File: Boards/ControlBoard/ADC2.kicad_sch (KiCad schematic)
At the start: 34 parts, among them IC3 MAX22530AWE+, IC4 MAX22530AWE+

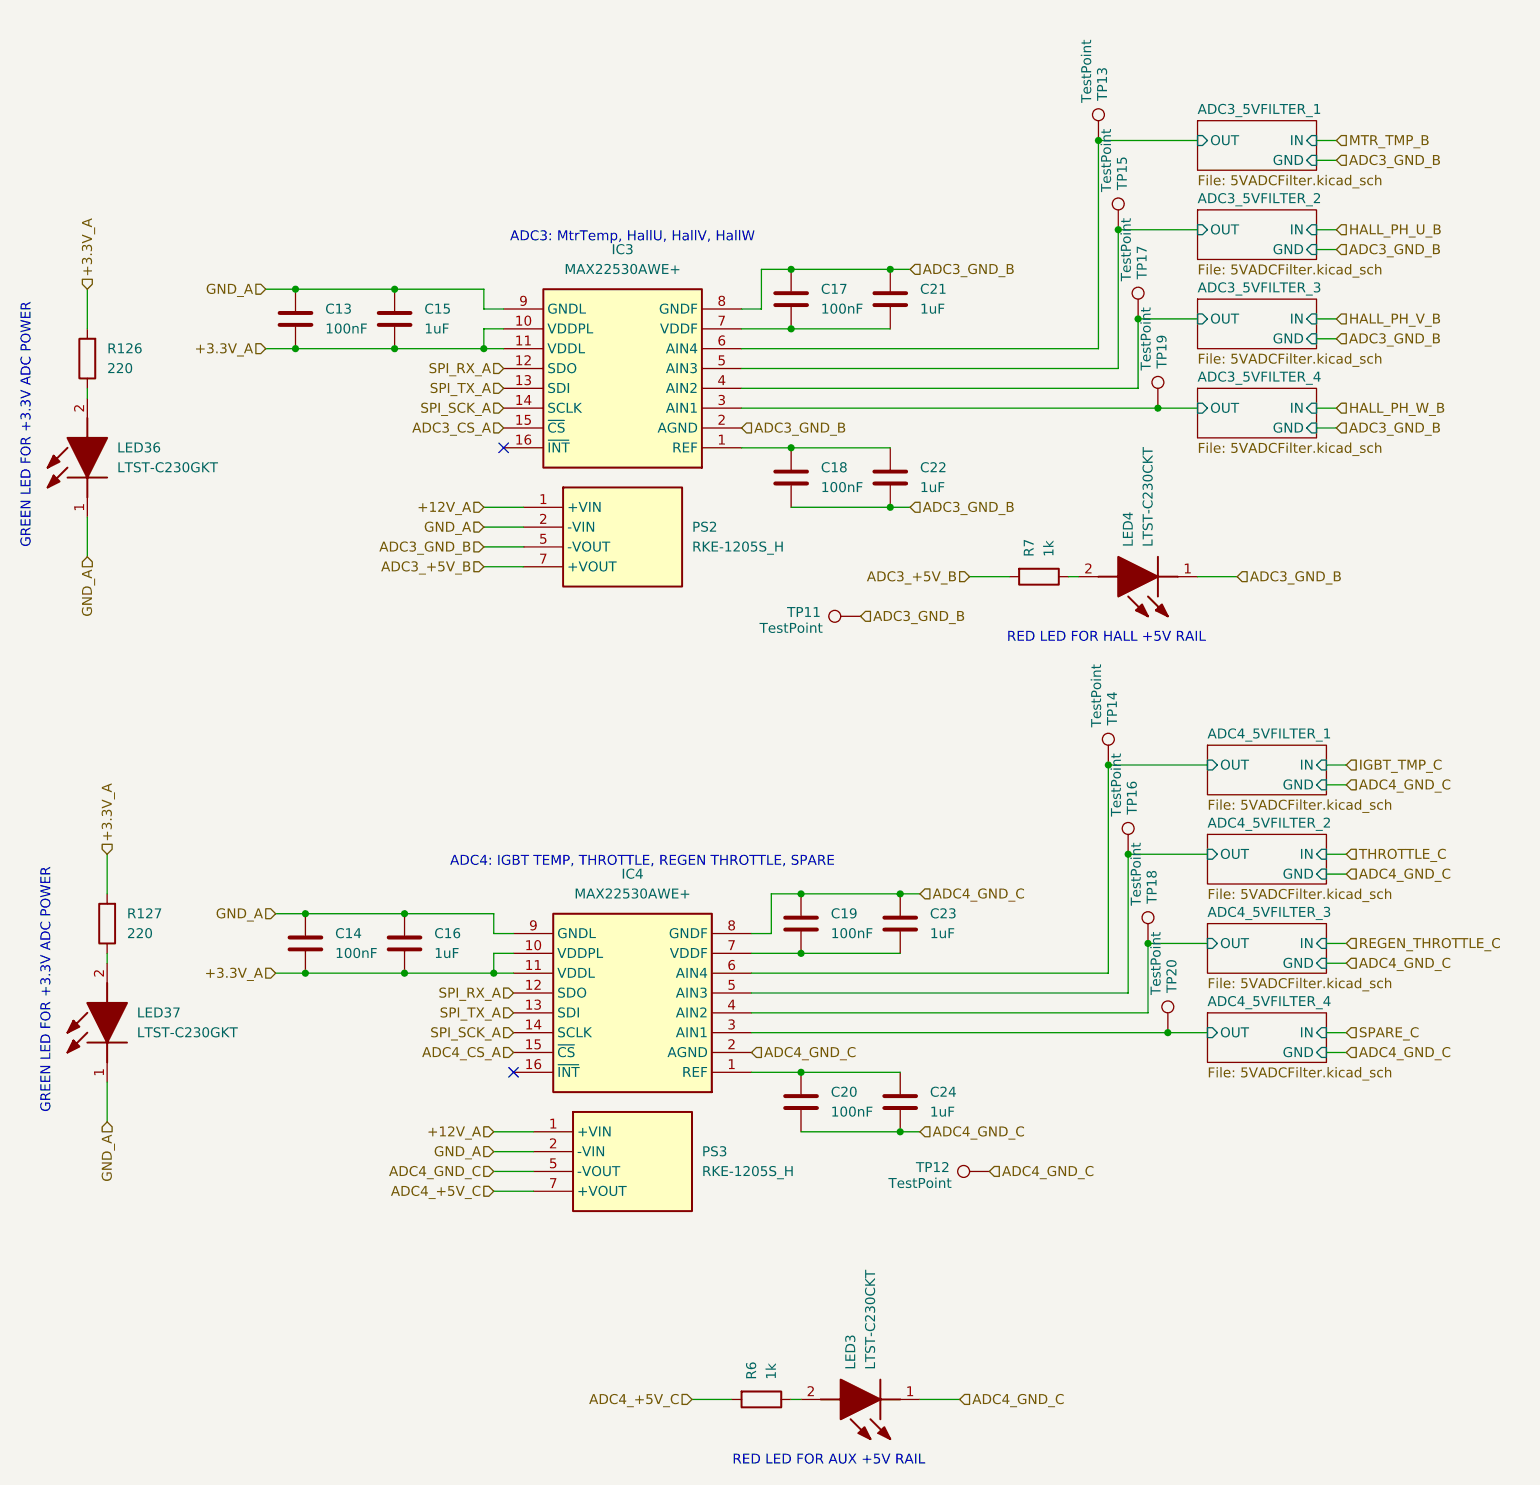
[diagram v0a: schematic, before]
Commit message: layout control boards, add baseplate, refine mechanical layout
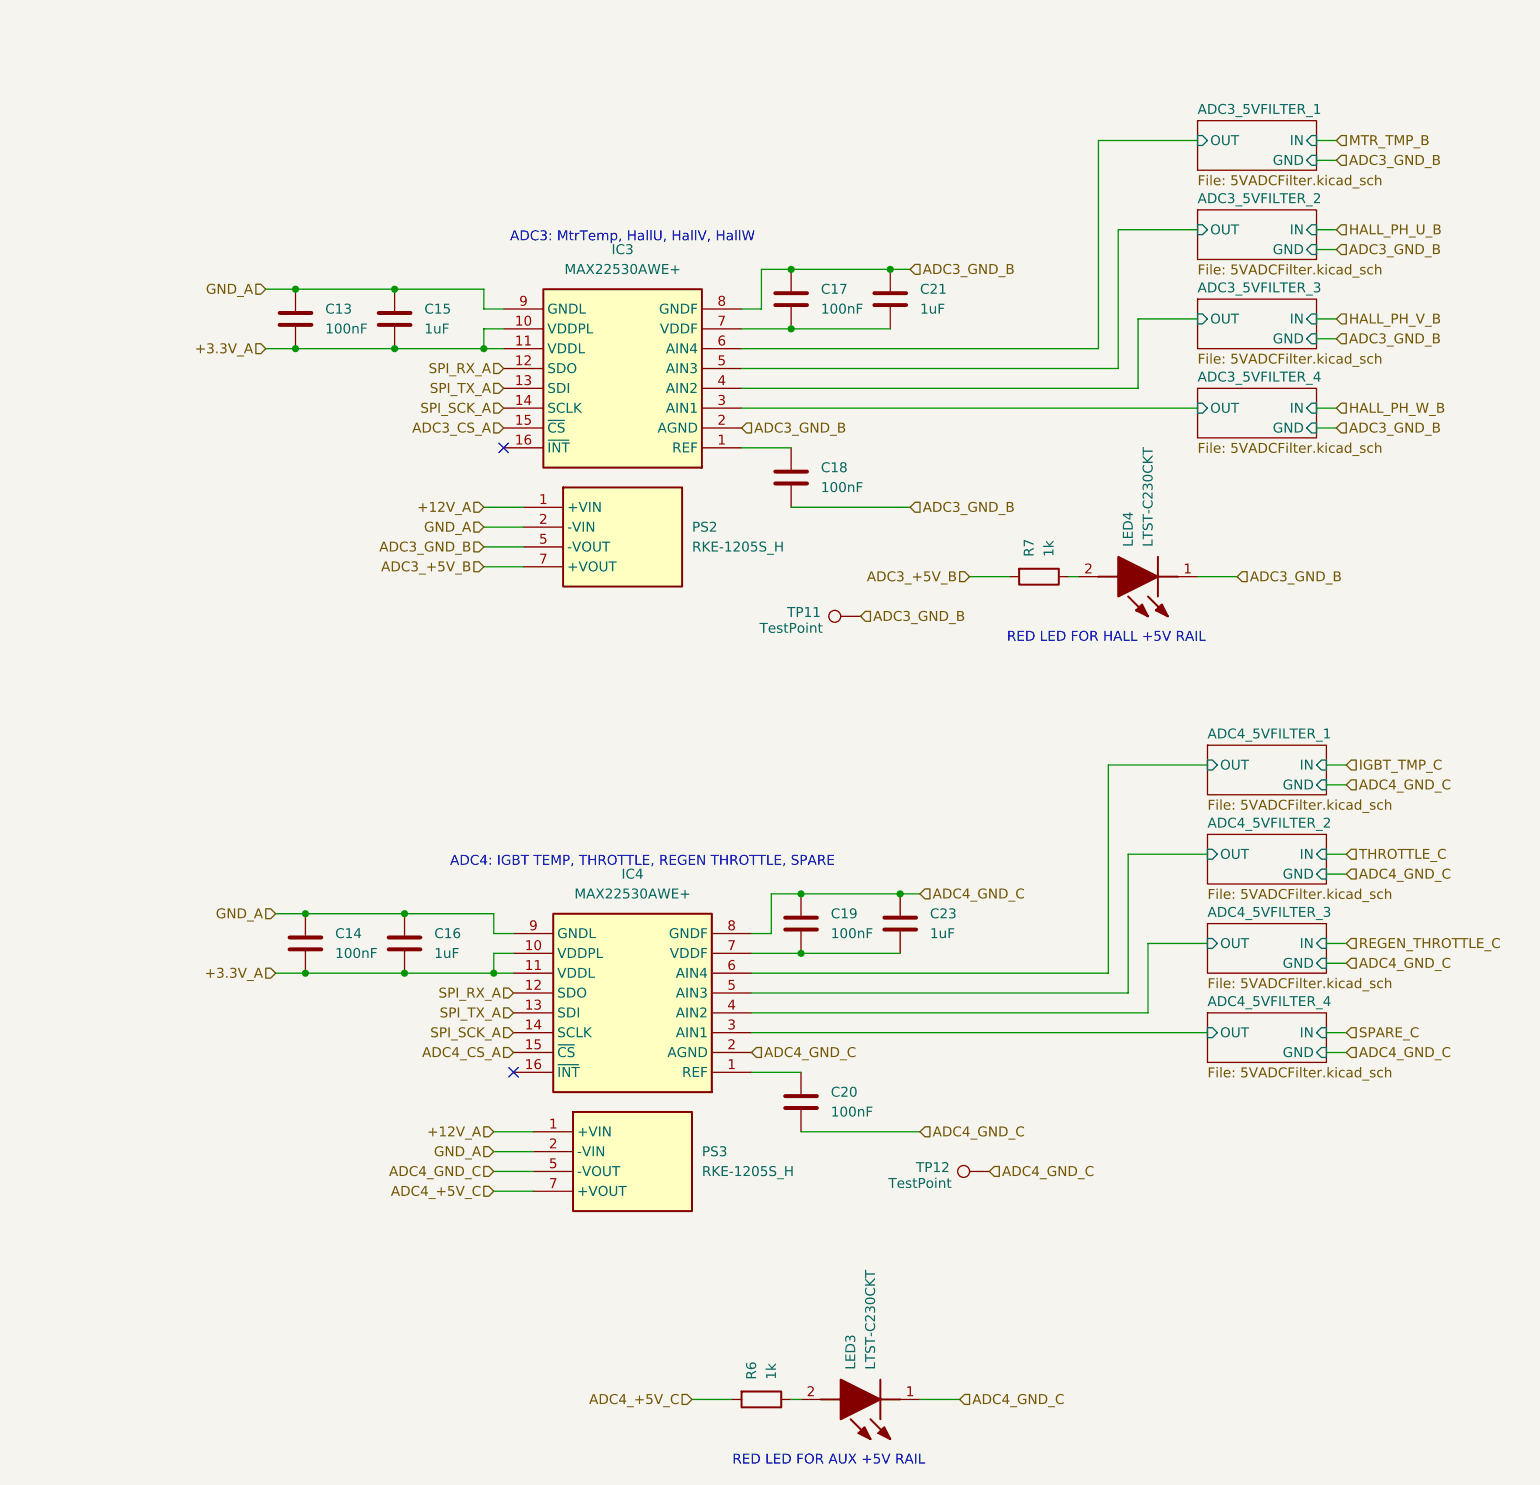
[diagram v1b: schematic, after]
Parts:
- removed C22, C24: 1uF, Capacitor_SMD:C_1210_3225Metric_Pad1.33x2.70mm_HandSolder, symbol Device:C
- removed LED36, LED37: LTST-C230GKT, InverterCom:LEDC3216X120N, symbol InverterCom:LTST-C230GKT
- removed R126, R127: 220, Resistor_SMD:R_1210_3225Metric_Pad1.30x2.65mm_HandSolder, symbol Device:R
- removed TP13, TP14, TP15, TP16, TP17, TP18, TP19, TP20: TestPoint, TestPoint:TestPoint_Loop_D2.54mm_Drill1.5mm_Beaded, symbol Connector:TestPoint
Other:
- note removed: "GREEN LED FOR +3.3V ADC POWER"
